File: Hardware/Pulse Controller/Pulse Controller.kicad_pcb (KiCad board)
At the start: 2 copper layers, 90.2 x 65.1 mm, 39 parts, among them J1 Serial, J2 RGB LED, J3 Arduino Out 1, J4 Arduino Out 2, J5 MOSFET Gates, J6 Signal In, P1 Power In, P2 PushButton, U1 ZSR330GTA, U2 ZSR500GTA, U3 4N35, U4 23LC1024, U5 LTC1855

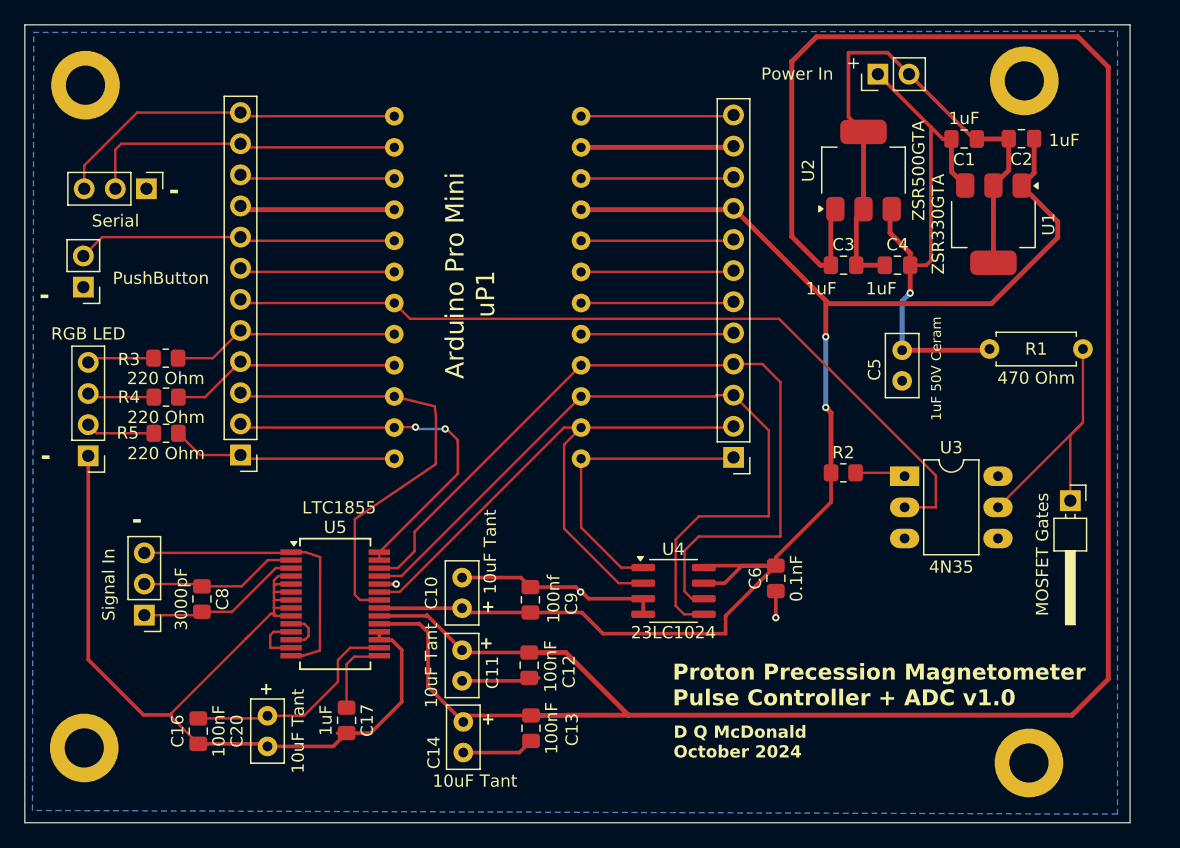
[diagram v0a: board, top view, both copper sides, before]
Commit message: Changed some Caps to SMD
Also fixed MISO and MOSI assignments
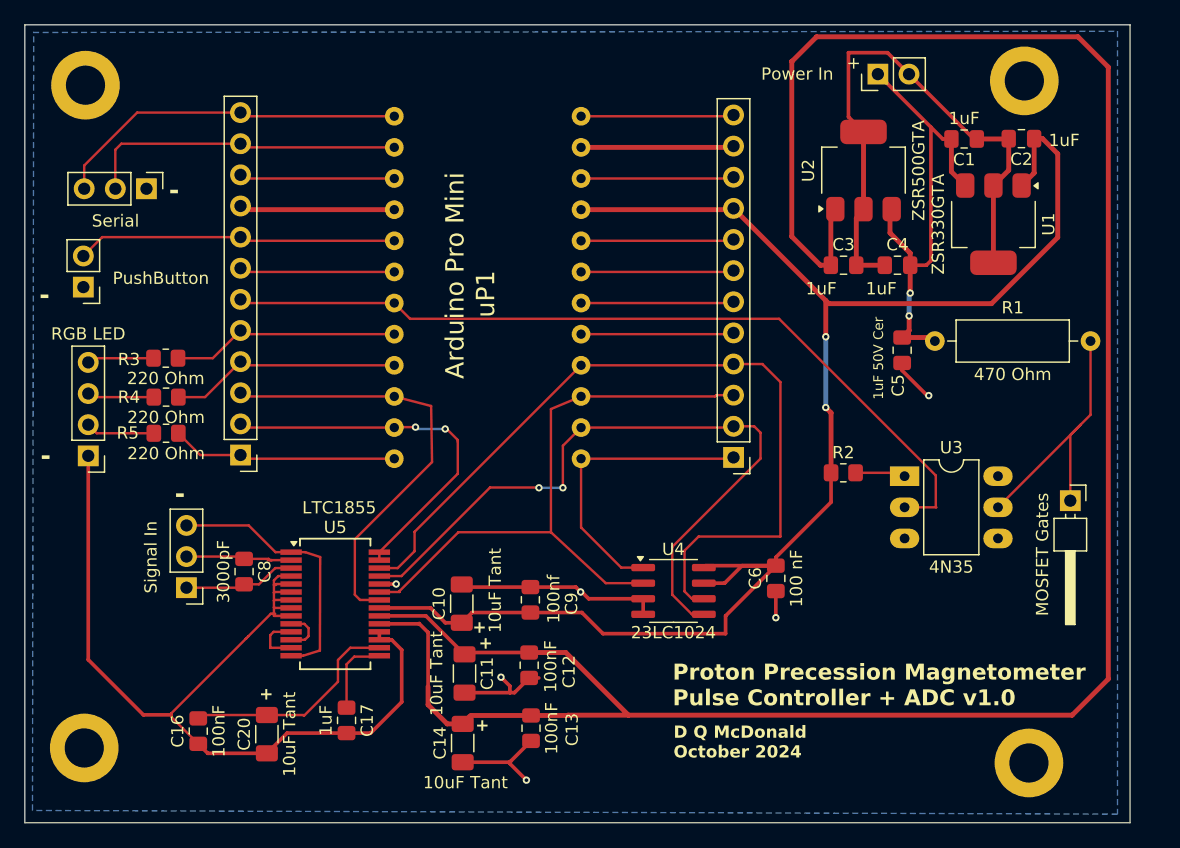
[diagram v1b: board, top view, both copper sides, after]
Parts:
- C10, C11, C14, C20: footprint Capacitor_THT:C_Disc_D5.0mm_W2.5mm_P2.50mm -> Capacitor_SMD:C_1206_3216Metric_Pad1.33x1.80mm_HandSolder
- C5: value 1uF 50V Ceram -> 1uF 50V Cer; footprint Capacitor_THT:C_Disc_D5.0mm_W2.5mm_P2.50mm -> Capacitor_SMD:C_0805_2012Metric_Pad1.18x1.45mm_HandSolder
- C6: value 0.1nF -> 100 nF
- R1: footprint Resistor_THT:R_Axial_DIN0207_L6.3mm_D2.5mm_P7.62mm_Horizontal -> Resistor_THT:R_Axial_DIN0309_L9.0mm_D3.2mm_P12.70mm_Horizontal
- moved R1 4.51 mm to (191.9, 78.2)
- moved C8 4.10 mm to (135.5, 97.1)
- moved J6 4.10 mm to (130.8, 98.4)
- moved C11 1.91 mm to (153.5, 105.4)
- moved C20 1.00 mm to (137.4, 110.3)
- moved C14 0.78 mm to (153.4, 111.0)
- moved C10 0.38 mm to (153.3, 99.7)
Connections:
- J4 pad 2: D11 -> MOSI
- J4 pad 3: D12 -> MISO
- U4 pad 2: D11 -> MISO
- U4 pad 5: D12 -> MOSI
- U5 pad 23: D11 -> MISO
- U5 pad 25: D12 -> MOSI
- uP1 pad 28: D12 -> MISO
- uP1 pad 29: D11 -> MOSI
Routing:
- net D12: track 62.5 -> 0.00 mm
- net MOSI: track 0.00 -> 57.9 mm, vias 0 -> 2
- net D11: track 51.6 -> 0.00 mm
- net MISO: track 0.00 -> 50.4 mm
- net +12V: track 45.0 -> 39.6 mm, vias 1 -> 2
- net AGND: track 207.0 -> 212.0 mm, vias 3 -> 6
- net +3.3V: track 126.5 -> 131.1 mm
- net Net-(J6-Pin_1): track 13.7 -> 9.35 mm
- net Net-(J6-Pin_2): track 12.9 -> 8.98 mm
- net +5V: track 191.0 -> 193.1 mm
- net D7: track 37.1 -> 36.0 mm
- net Net-(J5-Pin_1): track 22.4 -> 23.3 mm

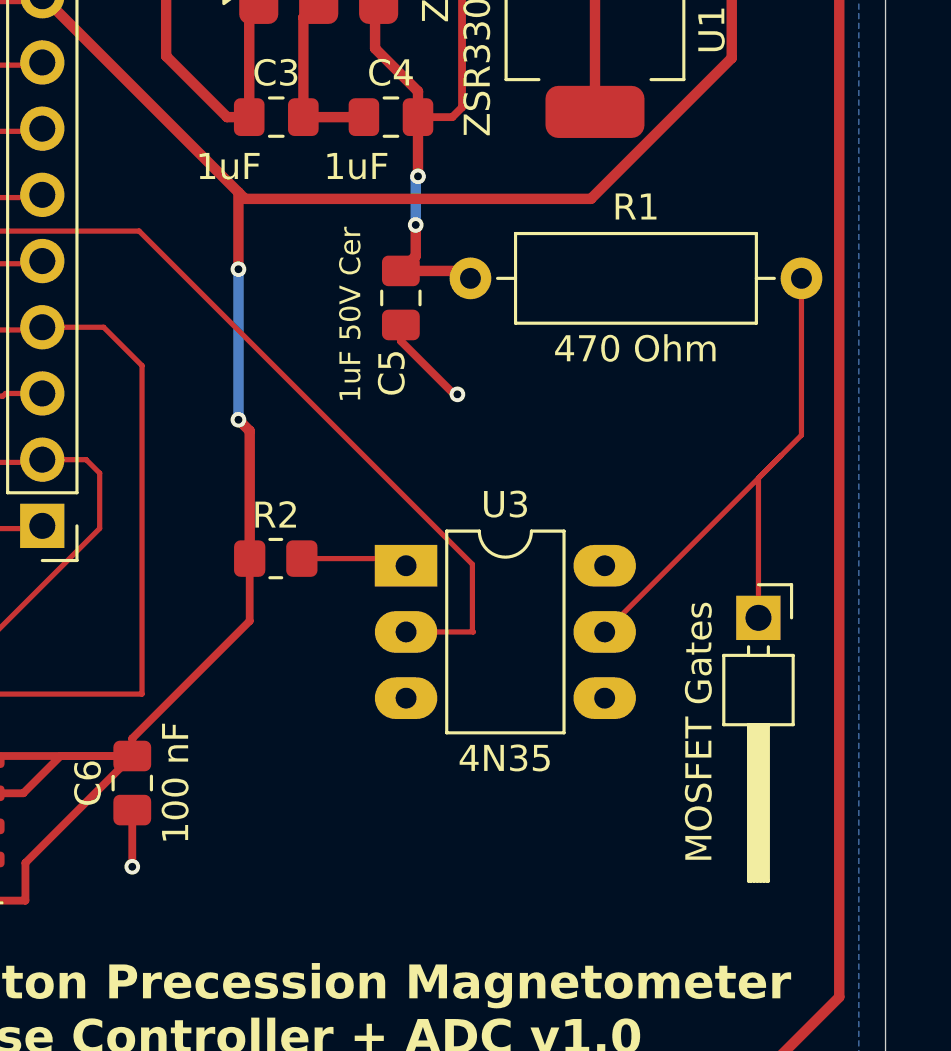
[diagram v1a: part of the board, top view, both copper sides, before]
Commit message: PCB for Pulse Controller
First complete schematic for Amplifier
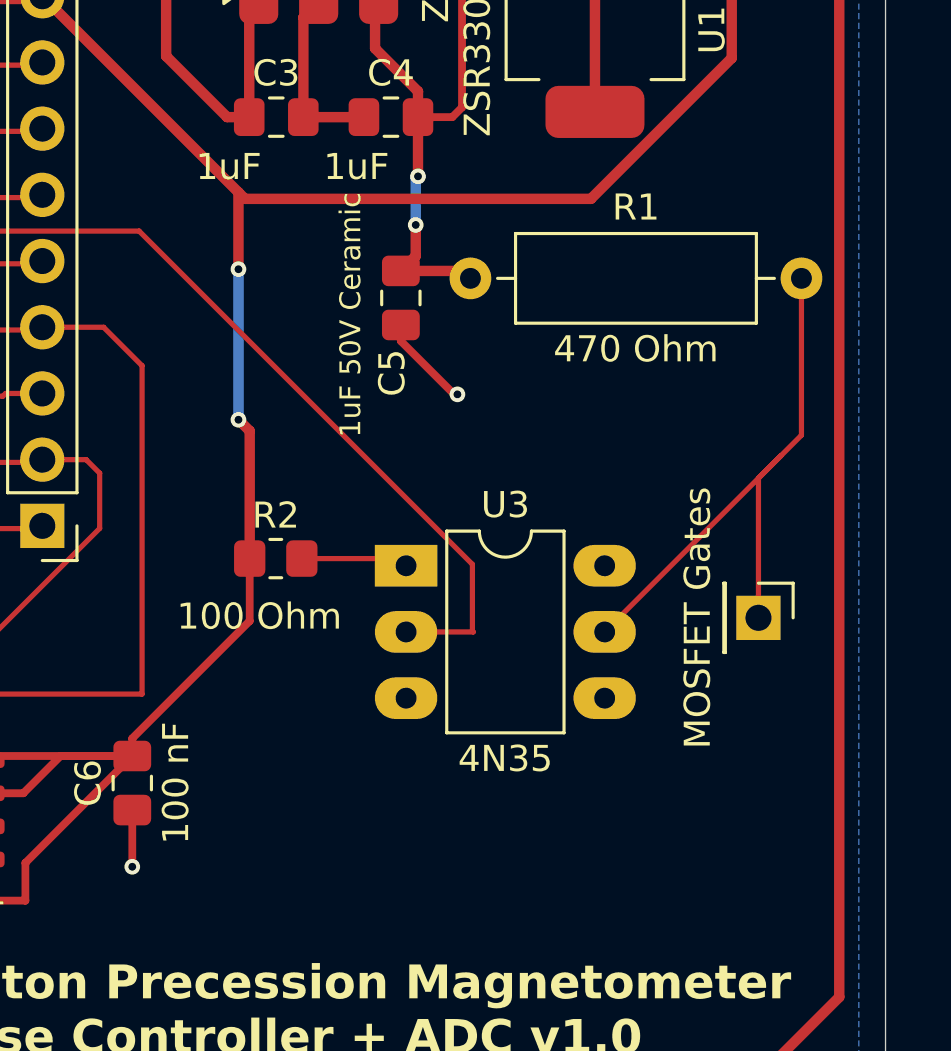
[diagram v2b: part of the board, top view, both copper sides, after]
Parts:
- C5: value 1uF 50V Cer -> 1uF 50V Ceramic
- J5: footprint Connector_PinHeader_2.54mm:PinHeader_1x01_P2.54mm_Horizontal -> Connector_PinHeader_2.54mm:PinHeader_1x01_P2.54mm_Vertical
- R2: value 220 Ohm -> 100 Ohm
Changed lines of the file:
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@@
 		)
 	)
-	(footprint "Connector_PinHeader_2.54mm:PinHeader_1x01_P2.54mm_Horizontal"
+	(footprint "Connector_PinHeader_2.54mm:PinHeader_1x01_P2.54mm_Vertical"
 		(layer "F.Cu")
 		(at 202.95 91.275 -90)
-		(descr "Through hole angled pin header, 1x01, 2.54mm pitch, 6mm pin length, single row")
-		(tags "Through hole angled pin header THT 1x01 2.54mm single row")
+		(descr "Through hole straight pin header, 1x01, 2.54mm pitch, single row")
+		(tags "Through hole pin header THT 1x01 2.54mm single row")
 		(property "Reference" "J5"
-			(at 4.385 -2.27 90)
+			(at 0 -2.33 90)
 			(layer "F.SilkS")
 			(hide yes)
@@
 		)
 		(property "Value" "MOSFET Gates"
-			(at 4.385 2.27 90)
+			(at 0 2.33 90)
 			(layer "F.SilkS")
 			(effects
@@
 			)
 		)
-		(property "Footprint" "Connector_PinHeader_2.54mm:PinHeader_1x01_P2.54mm_Horizontal"
+		(property "Footprint" "Connector_PinHeader_2.54mm:PinHeader_1x01_P2.54mm_Vertical"
 			(at 0 0 -90)
 			(unlocked yes)
@@
 		(attr through_hole)
 		(fp_line
-			(start 1.44 1.33)
-			(end 4.1 1.33)
-			(stroke
-				(width 0.12)
-				(type solid)
-			)
-			(layer "F.SilkS")
-		)
-		(fp_line
-			(start 4.1 1.33)
-			(end 4.1 -1.33)
-			(stroke
-				(width 0.12)
-				(type solid)
-			)
-			(layer "F.SilkS")
-		)
-		(fp_line
-			(start 1.11 0.38)
-			(end 1.44 0.38)
-			(stroke
-				(width 0.12)
-				(type solid)
-			)
-			(layer "F.SilkS")
-		)
-		(fp_line
-			(start 10.1 0.38)
-			(end 4.1 0.38)
-			(stroke
-				(width 0.12)
-				(type solid)
-			)
-			(layer "F.SilkS")
-		)
-		(fp_line
-			(start 4.1 0.28)
-			(end 10.1 0.28)
+			(start -1.33 1.33)
+			(end 1.33 1.33)
 			(stroke
 				(width 0.12)
@@
 		)
 		(fp_line
-			(start 4.1 0.16)
-			(end 10.1 0.16)
-			(stroke
-				(width 0.12)
-				(type solid)
-			)
-			(layer "F.SilkS")
-		)
-		(fp_line
-			(start 4.1 0.04)
-			(end 10.1 0.04)
-			(stroke
-				(width 0.12)
-				(type solid)
-			)
-			(layer "F.SilkS")
-		)
-		(fp_line
-			(start -1.27 0)
-			(end -1.27 -1.27)
-			(stroke
-				(width 0.12)
-				(type solid)
-			)
-			(layer "F.SilkS")
-		)
-		(fp_line
-			(start 4.1 -0.08)
-			(end 10.1 -0.08)
-			(stroke
-				(width 0.12)
-				(type solid)
-			)
-			(layer "F.SilkS")
-		)
-		(fp_line
-			(start 4.1 -0.2)
-			(end 10.1 -0.2)
-			(stroke
-				(width 0.12)
-				(type solid)
-			)
-			(layer "F.SilkS")
-		)
-		(fp_line
-			(start 4.1 -0.32)
-			(end 10.1 -0.32)
-			(stroke
-				(width 0.12)
-				(type solid)
-			)
-			(layer "F.SilkS")
-		)
-		(fp_line
-			(start 1.11 -0.38)
-			(end 1.44 -0.38)
-			(stroke
-				(width 0.12)
-				(type solid)
-			)
-			(layer "F.SilkS")
-		)
-		(fp_line
-			(start 4.1 -0.38)
-			(end 10.1 -0.38)
+			(start -1.33 1.27)
+			(end -1.33 1.33)
 			(stroke
 				(width 0.12)
@@
 		)
 		(fp_line
-			(start 10.1 -0.38)
-			(end 10.1 0.38)
+			(start -1.33 1.27)
+			(end 1.33 1.27)
 			(stroke
 				(width 0.12)
@@
 		)
 		(fp_line
-			(start -1.27 -1.27)
-			(end 0 -1.27)
+			(start 1.33 1.27)
+			(end 1.33 1.33)
 			(stroke
 				(width 0.12)
@@
 		)
 		(fp_line
-			(start 1.44 -1.33)
-			(end 1.44 1.33)
+			(start -1.33 0)
+			(end -1.33 -1.33)
 			(stroke
 				(width 0.12)
@@
 		)
 		(fp_line
-			(start 4.1 -1.33)
-			(end 1.44 -1.33)
+			(start -1.33 -1.33)
+			(end 0 -1.33)
 			(stroke
 				(width 0.12)
@@
 		(fp_line
 			(start -1.8 1.8)
-			(end 10.55 1.8)
+			(end 1.8 1.8)
 			(stroke
 				(width 0.05)
@@
 		)
 		(fp_line
-			(start 10.55 1.8)
-			(end 10.55 -1.8)
+			(start 1.8 1.8)
+			(end 1.8 -1.8)
 			(stroke
 				(width 0.05)
@@
 		)
 		(fp_line
-			(start 10.55 -1.8)
+			(start 1.8 -1.8)
 			(end -1.8 -1.8)
 			(stroke
@@
 		)
 		(fp_line
-			(start 1.5 1.27)
-			(end 1.5 -0.635)
-			(stroke
-				(width 0.1)
-				(type solid)
-			)
-			(layer "F.Fab")
-		)
-		(fp_line
-			(start 4.04 1.27)
-			(end 1.5 1.27)
-			(stroke
-				(width 0.1)
-				(type solid)
-			)
-			(layer "F.Fab")
-		)
-		(fp_line
-			(start -0.32 0.32)
-			(end 1.5 0.32)
-			(stroke
-				(width 0.1)
-				(type solid)
-			)
-			(layer "F.Fab")
-		)
-		(fp_line
-			(start 4.04 0.32)
-			(end 10.04 0.32)
-			(stroke
-				(width 0.1)
-				(type solid)
-			)
-			(layer "F.Fab")
-		)
-		(fp_line
-			(start -0.32 -0.32)
-			(end -0.32 0.32)
-			(stroke
-				(width 0.1)
-				(type solid)
-			)
-			(layer "F.Fab")
-		)
-		(fp_line
-			(start -0.32 -0.32)
-			(end 1.5 -0.32)
-			(stroke
-				(width 0.1)
-				(type solid)
-			)
-			(layer "F.Fab")
-		)
-		(fp_line
-			(start 4.04 -0.32)
-			(end 10.04 -0.32)
+			(start -1.27 1.27)
+			(end -1.27 -0.635)
 			(stroke
 				(width 0.1)
@@
 		)
 		(fp_line
-			(start 10.04 -0.32)
-			(end 10.04 0.32)
+			(start 1.27 1.27)
+			(end -1.27 1.27)
 			(stroke
 				(width 0.1)
@@
 		)
 		(fp_line
-			(start 1.5 -0.635)
-			(end 2.135 -1.27)
+			(start -1.27 -0.635)
+			(end -0.635 -1.27)
 			(stroke
 				(width 0.1)
@@
 		)
 		(fp_line
-			(start 2.135 -1.27)
-			(end 4.04 -1.27)
+			(start -0.635 -1.27)
+			(end 1.27 -1.27)
 			(stroke
 				(width 0.1)
@@
 		)
 		(fp_line
-			(start 4.04 -1.27)
-			(end 4.04 1.27)
+			(start 1.27 -1.27)
+			(end 1.27 1.27)
 			(stroke
 				(width 0.1)
@@
 		)
 		(fp_text user "${REFERENCE}"
-			(at 2.77 0 0)
+			(at 0 0 0)
 			(layer "F.Fab")
 			(effects
@@
 			(pintype "passive")
 		)
-		(model "${KICAD8_3DMODEL_DIR}/Connector_PinHeader_2.54mm.3dshapes/PinHeader_1x01_P2.54mm_Horizontal.wrl"
+		(model "${KICAD8_3DMODEL_DIR}/Connector_PinHeader_2.54mm.3dshapes/PinHeader_1x01_P2.54mm_Vertical.wrl"
 			(offset
 				(xyz 0 0 0)
@@
 			)
 		)
-		(property "Value" "220 Ohm"
-			(at 0 1.65 0)
-			(layer "F.Fab")
+		(property "Value" "100 Ohm"
+			(at -0.63 2.22375 0)
+			(layer "F.SilkS")
 			(effects
 				(font
@@
 			)
 		)
-		(property "Value" "1uF 50V Cer"
-			(at 0.64875 1.93 270)
+		(property "Value" "1uF 50V Ceramic"
+			(at 0.64875 1.93 -90)
 			(layer "F.SilkS")
 			(effects
@@
 	)
 	(segment
-		(start 203.808125 85.058125)
+		(start 202.95 91.275)
 		(end 202.95 85.91625)
 		(width 0.2)
@@
 	)
 	(segment
-		(start 202.95 85.91625)
-		(end 202.95 91.275)
+		(start 203.808125 85.058125)
+		(end 197.05 91.81625)
 		(width 0.2)
 		(layer "F.Cu")
@@
 	)
 	(segment
-		(start 203.808125 85.058125)
-		(end 197.05 91.81625)
+		(start 202.95 85.91625)
+		(end 203.808125 85.058125)
 		(width 0.2)
 		(layer "F.Cu")
